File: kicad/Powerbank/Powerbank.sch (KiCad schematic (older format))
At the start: 8 parts

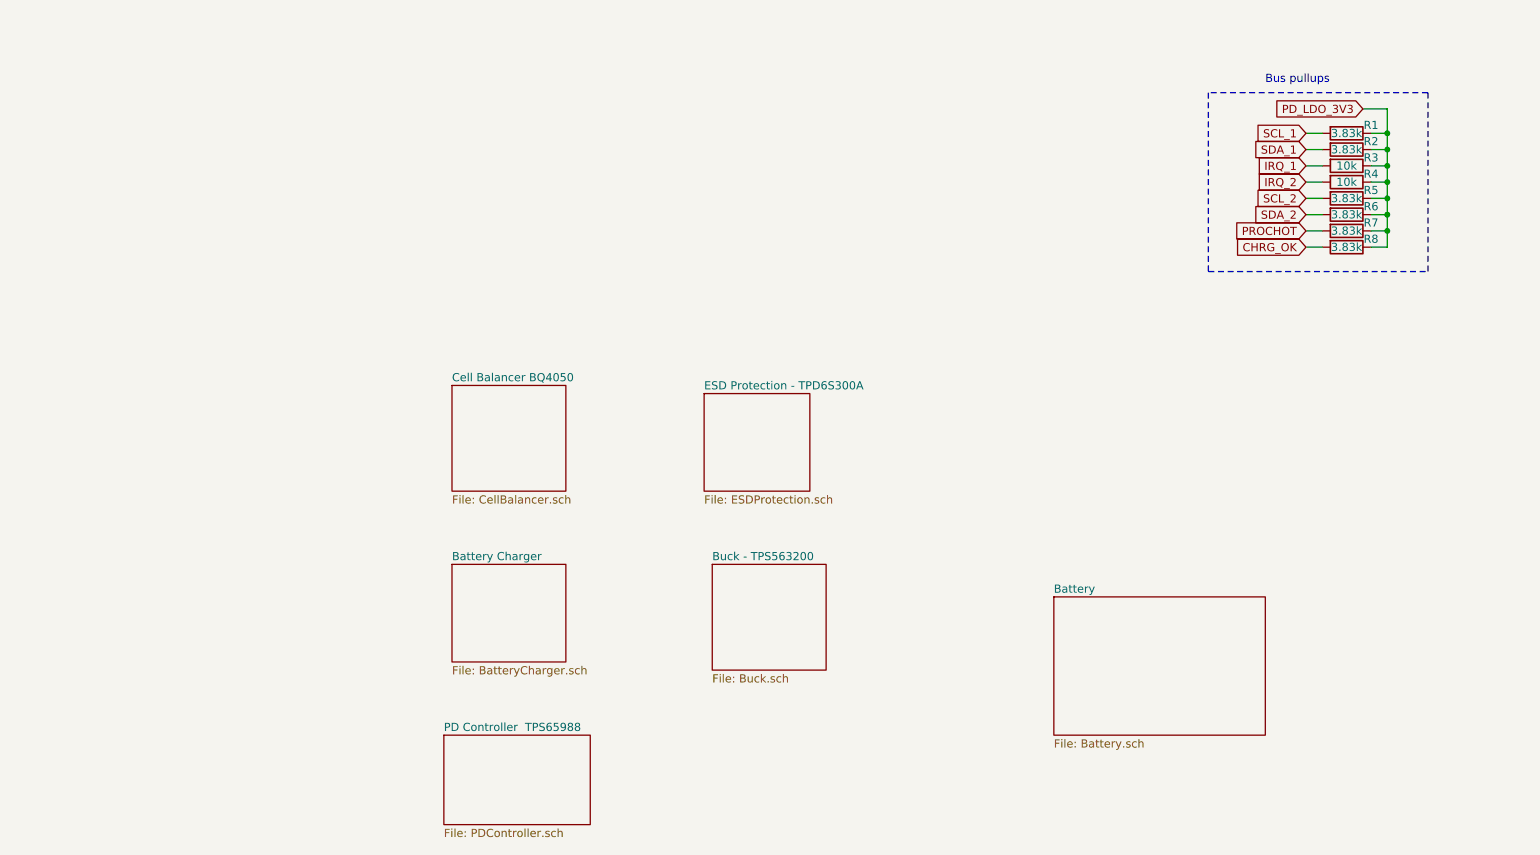
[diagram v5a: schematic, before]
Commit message: Updated layout in schematic for nicer look
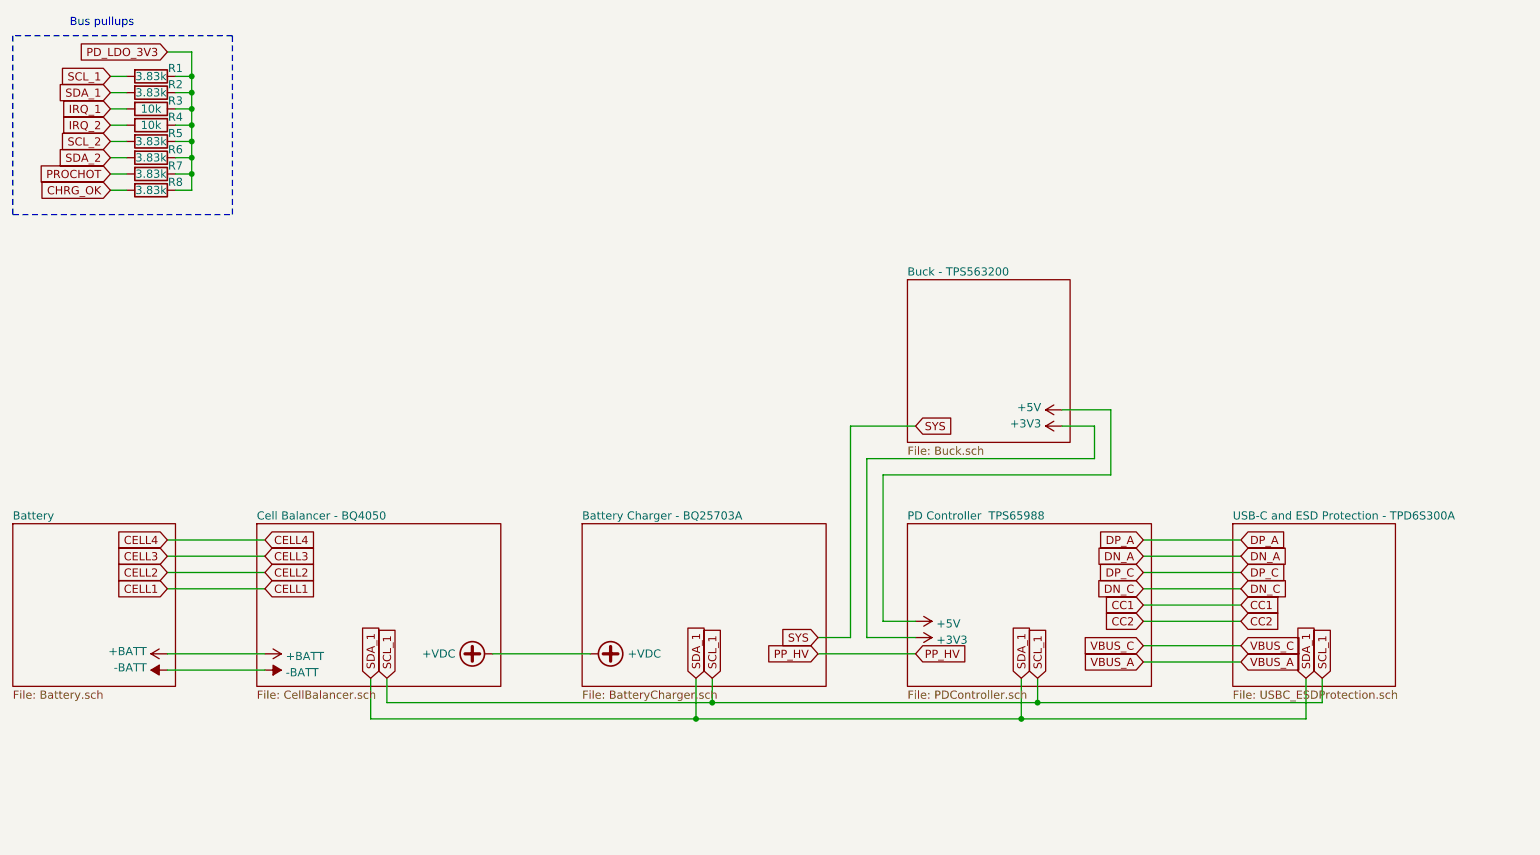
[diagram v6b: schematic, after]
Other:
- moved on the sheet: R1, R2, R3, R4, R5, R6, R7, R8
